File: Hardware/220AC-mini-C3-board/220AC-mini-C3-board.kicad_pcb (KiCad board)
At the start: 2 copper layers, 52.7 x 52.7 mm, 18 parts, among them J1 AC MAINS POWER, J2 ON/OFF switch, J3 Conn_01x04, K1 HF163-F, Q1 Q_NPN_CBE, Q2 Q_NPN_CBE, U1 PBO-3C-3

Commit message: Update silkscreen
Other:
- board text added: "↗"
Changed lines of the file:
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@@
     (property "Sheetname" "")
     (attr through_hole)
-    (fp_text reference "K1" (at 0 8.5965 90) (layer "F.SilkS")
+    (fp_text reference "K1" (at -6.22 -0.84 180) (layer "F.SilkS")
       (effects (font (size 1 1) (thickness 0.15)))
     )
@@
     (effects (font (size 1 1) (thickness 0.15)))
   )
-  (gr_text "Latch relay" (at 132.03 107.8) (layer "F.SilkS")
+  (gr_text "Latch relay" (at 132.03 107.8275) (layer "F.SilkS")
     (effects (font (size 1 1) (thickness 0.14)))
   )
@@
     (effects (font (size 1.5 1.5) (thickness 0.25)) (justify left))
   )
-  (gr_text "max. 900W" (at 146.58 104.79 90) (layer "F.SilkS")
+  (gr_text "max. 900W" (at 142.67 107.82) (layer "F.SilkS")
     (effects (font (size 1 1) (thickness 0.15)))
   )
+  (gr_text "↗" (at 147.63 105.85) (layer "F.SilkS")
+    (effects (font (size 2 2) (thickness 0.15)))
+  )
   (gr_text "GND" (at 114.03 87.16) (layer "F.SilkS")

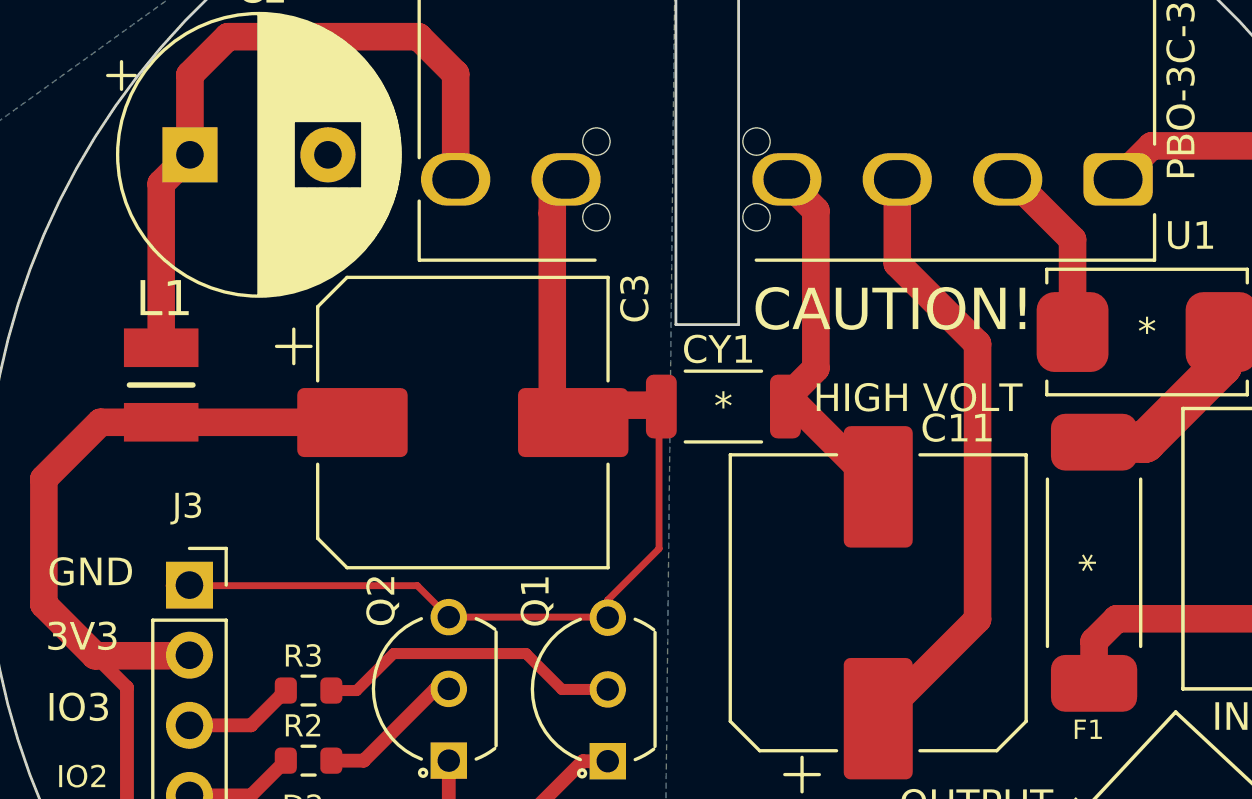
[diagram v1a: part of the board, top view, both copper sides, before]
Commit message: Remove innecesary GND since there is ground pane
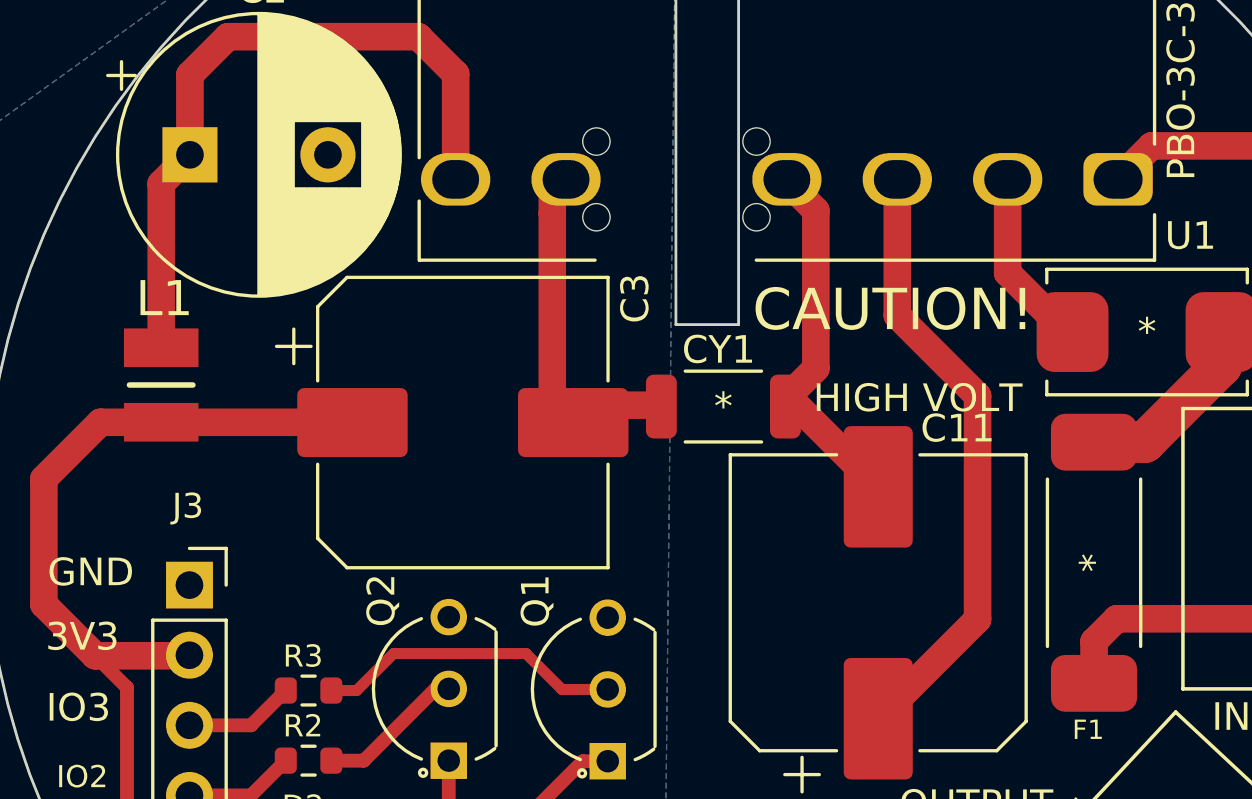
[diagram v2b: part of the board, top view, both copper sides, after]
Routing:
- net GND: track 37.4 -> 12.6 mm
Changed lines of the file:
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@@
     (effects (font (size 1 1) (thickness 0.15)))
   )
-  (segment (start 143.25 75.97) (end 143.25 72.92) (width 1) (layer "F.Cu") (net 1))
+  (segment (start 146.16 80.76) (end 143.25 77.85) (width 1) (layer "F.Cu") (net 1))
+  (segment (start 143.25 77.85) (end 143.25 72.92) (width 1) (layer "F.Cu") (net 1))
   (segment (start 142.56 92.46) (end 146.16 88.86) (width 1) (layer "F.Cu") (net 1))
-  (segment (start 146.16 88.86) (end 146.16 78.88) (width 1) (layer "F.Cu") (net 1))
-  (segment (start 146.16 78.88) (end 143.25 75.97) (width 1) (layer "F.Cu") (net 1))
+  (segment (start 146.16 88.86) (end 146.16 80.76) (width 1) (layer "F.Cu") (net 1))
   (segment (start 139.390001 73.14) (end 140.300001 74.05) (width 1) (layer "F.Cu") (net 2))
   (segment (start 140.300001 74.05) (end 140.3 79.7679) (width 1) (layer "F.Cu") (net 2))
@@
   (segment (start 117.622323 69.127677) (end 117.622323 72.03) (width 1) (layer "F.Cu") (net 3))
   (segment (start 125.9 67.75) (end 119 67.75) (width 1) (layer "F.Cu") (net 3))
-  (segment (start 134.62 86.3) (end 134.62 81.2321) (width 0.25) (layer "F.Cu") (net 4))
-  (segment (start 132.76 88.8) (end 132.76 88.16) (width 0.25) (layer "F.Cu") (net 4))
-  (segment (start 127 88.78) (end 132.74 88.78) (width 0.25) (layer "F.Cu") (net 4))
-  (segment (start 125.86 87.64) (end 127 88.78) (width 0.25) (layer "F.Cu") (net 4))
   (segment (start 130.75 73.420001) (end 131.250001 72.92) (width 1) (layer "F.Cu") (net 4))
   (segment (start 131.28 81.68) (end 130.75 81.15) (width 1) (layer "F.Cu") (net 4))
   (segment (start 130.75 81.15) (end 130.75 74.15) (width 1) (layer "F.Cu") (net 4))
-  (segment (start 116.865 87.64) (end 125.86 87.64) (width 0.25) (layer "F.Cu") (net 4))
   (segment (start 131.86 81.1) (end 131.28 81.68) (width 1) (layer "F.Cu") (net 4))
-  (segment (start 134.62 81.2321) (end 134.7021 81.15) (width 0.25) (layer "F.Cu") (net 4))
   (segment (start 134.4721 81.1) (end 131.86 81.1) (width 1) (layer "F.Cu") (net 4))
   (segment (start 130.75 74.15) (end 130.75 73.420001) (width 1) (layer "F.Cu") (net 4))
-  (segment (start 132.76 88.16) (end 134.62 86.3) (width 0.25) (layer "F.Cu") (net 4))
-  (segment (start 132.74 88.78) (end 132.76 88.8) (width 0.25) (layer "F.Cu") (net 4))
   (segment (start 151.2 88.84) (end 150.38 89.66) (width 1) (layer "F.Cu") (net 5))
   (segment (start 150.38 89.66) (end 150.38 91.1788) (width 1) (layer "F.Cu") (net 5))
@@
   (segment (start 156.906068 71.706068) (end 152.463931 71.706068) (width 1) (layer "F.Cu") (net 7))
   (arc (start 159.835 78.777136) (mid 159.073795 74.950302) (end 156.906068 71.706068) (width 1) (layer "F.Cu") (net 7))
-  (segment (start 147.42 72.92) (end 149.60125 75.10125) (width 1) (layer "F.Cu") (net 8))
-  (segment (start 147.25 72.92) (end 147.42 72.92) (width 1) (layer "F.Cu") (net 8))
-  (segment (start 149.60125 75.10125) (end 149.60125 78.45) (width 1) (layer "F.Cu") (net 8))
+  (segment (start 149.60125 78.45) (end 149.39 78.45) (width 1) (layer "F.Cu") (net 8))
+  (segment (start 149.39 78.45) (end 147.25 76.31) (width 1) (layer "F.Cu") (net 8))
+  (segment (start 147.25 76.31) (end 147.25 72.92) (width 1) (layer "F.Cu") (net 8))
   (segment (start 119.835 95.24) (end 121.095 93.98) (width 0.5) (layer "F.Cu") (net 9))
   (segment (start 117.605 95.24) (end 119.835 95.24) (width 0.5) (layer "F.Cu") (net 9))

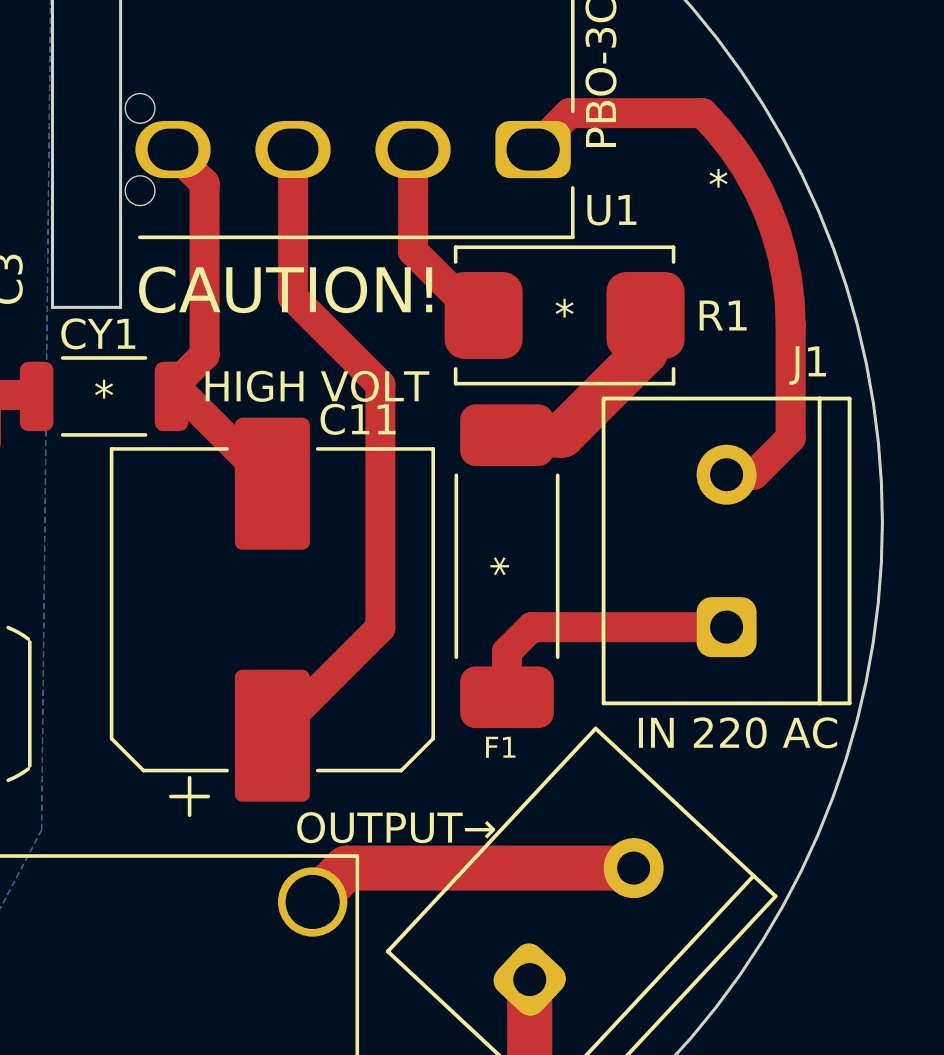
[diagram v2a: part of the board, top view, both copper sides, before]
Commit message: H 220AC adapter silk
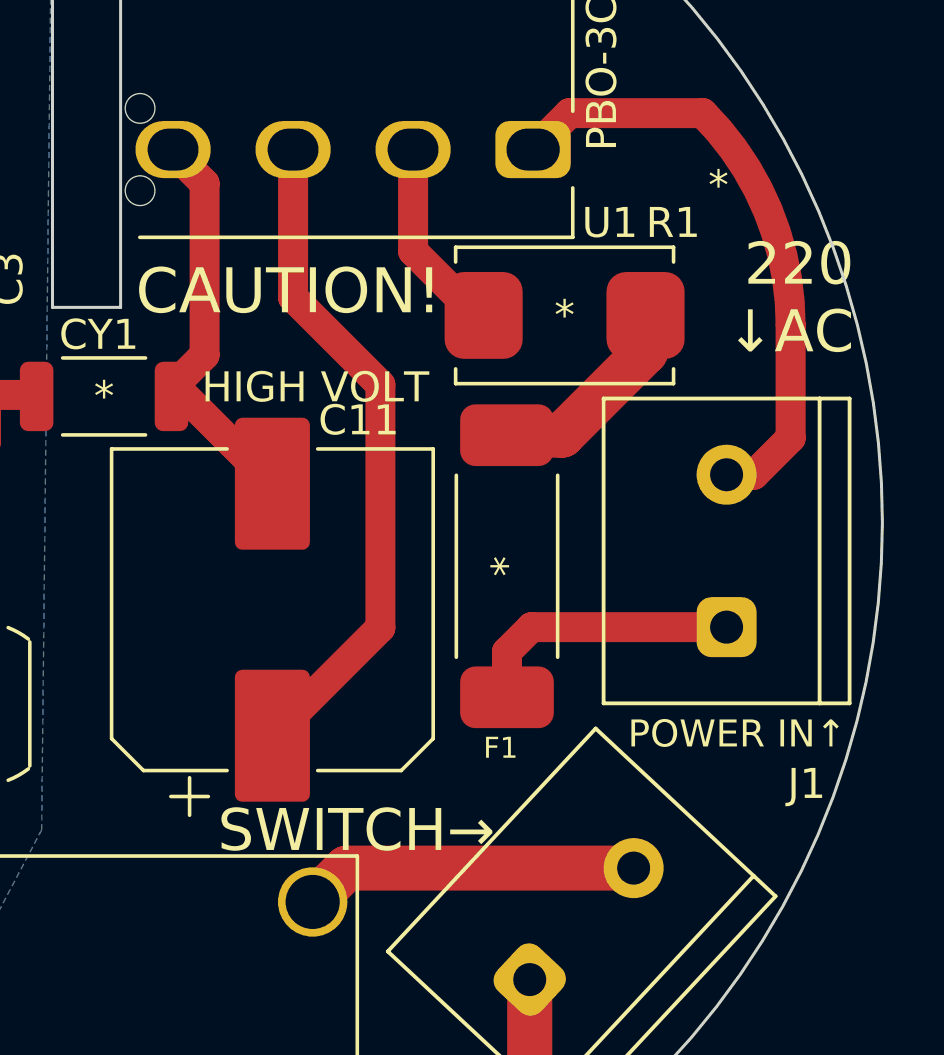
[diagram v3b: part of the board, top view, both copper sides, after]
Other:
- board text added: "220 ↓AC"
- board text added: "POWER IN↑"
- board text added: "SWITCH→"
- board text removed: "IN 220 AC"
- board text removed: "OUTPUT→"
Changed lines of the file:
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@@
     (property "Sheetname" "")
     (attr through_hole)
-    (fp_text reference "R1" (at -5.28 -0.04 180) (layer "F.SilkS")
+    (fp_text reference "R1" (at -3.62 3.08 180) (layer "F.SilkS")
       (effects (font (size 1 1) (thickness 0.15)))
     )
@@
     (property "Sheetname" "")
     (attr through_hole)
-    (fp_text reference "U1" (at -2.630001 -2.05) (layer "F.SilkS")
+    (fp_text reference "U1" (at -2.560001 -2.45) (layer "F.SilkS")
       (effects (font (size 1 1) (thickness 0.15)))
     )
@@
     (property "Sheetname" "")
     (attr through_hole)
-    (fp_text reference "J1" (at 6.28 2.8 180) (layer "F.SilkS")
+    (fp_text reference "J1" (at -7.77 2.67 180) (layer "F.SilkS")
       (effects (font (size 1.002039 1.002039) (thickness 0.15)))
     )
@@
     (effects (font (size 1.5 1.5) (thickness 0.25)) (justify left mirror))
   )
-  (gr_text "OUTPUT→" (at 146.68 95.56) (layer "F.SilkS")
-    (effects (font (size 1 1) (thickness 0.15)))
-  )
-  (gr_text "IN 220 AC" (at 158.05 92.4) (layer "F.SilkS")
-    (effects (font (size 1 1) (thickness 0.15)))
+  (gr_text "SWITCH→" (at 145.36 95.62) (layer "F.SilkS")
+    (effects (font (size 1.4 1.4) (thickness 0.15)))
+  )
+  (gr_text "POWER IN↑" (at 158.05 92.4) (layer "F.SilkS")
+    (effects (font (size 0.9 0.9) (thickness 0.15)))
   )
   (gr_text "Latch relay" (at 132.03 107.8275) (layer "F.SilkS")
@@
     (effects (font (size 1 1) (thickness 0.15)) (justify left))
   )
+  (gr_text "220 \n↓AC" (at 161.95 77.87) (layer "F.SilkS")
+    (effects (font (size 1.4 1.4) (thickness 0.15)) (justify right))
+  )
   (gr_text "CAUTION!" (at 138 77.65) (layer "F.SilkS")

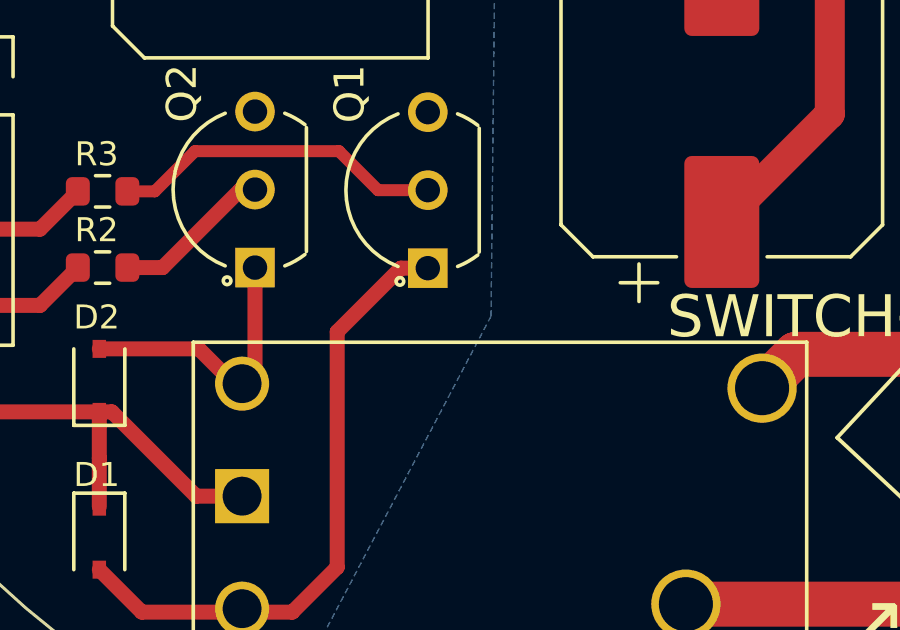
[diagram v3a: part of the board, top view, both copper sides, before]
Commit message: Update pcf8563 switch
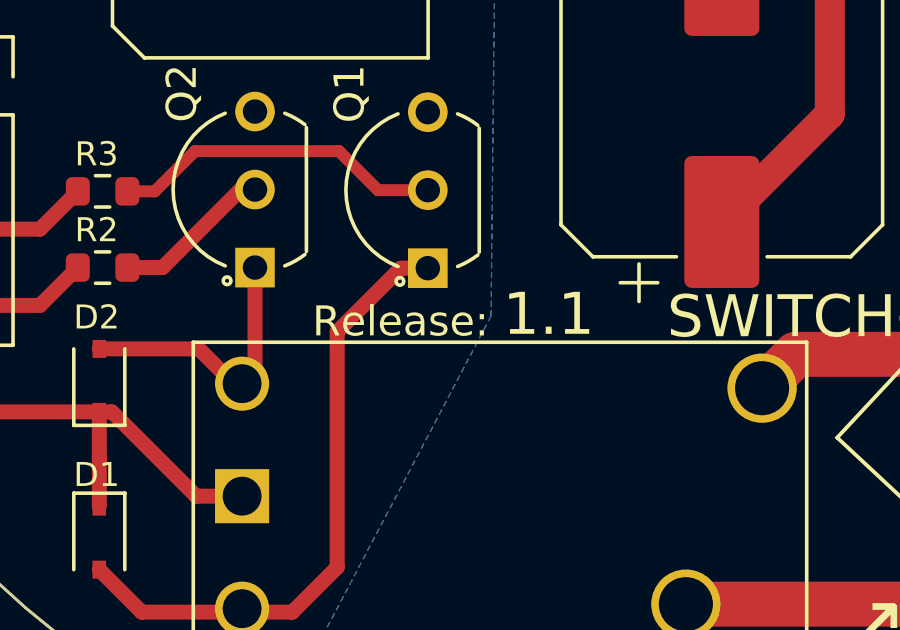
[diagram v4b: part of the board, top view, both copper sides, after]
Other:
- board text added: "1.1"
- board text added: "Release:"
